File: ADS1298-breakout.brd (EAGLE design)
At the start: 63.5 x 25.4 mm, 31 parts, among them IC2 TPS73250DBVT, IC3 TPS73233DBVT

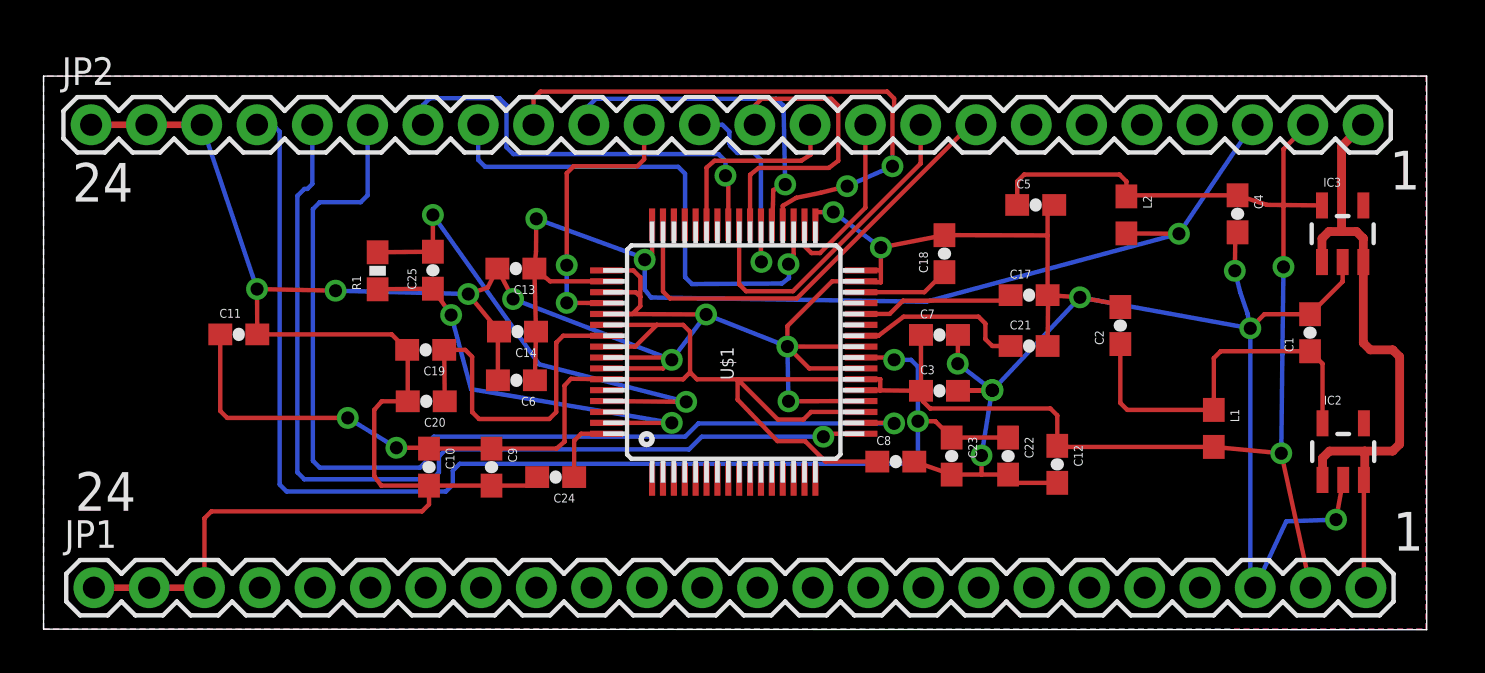
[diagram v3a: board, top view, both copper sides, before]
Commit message: fixed pin spacing so it is 0.1 inch; fixed board outline so it is even on all edges
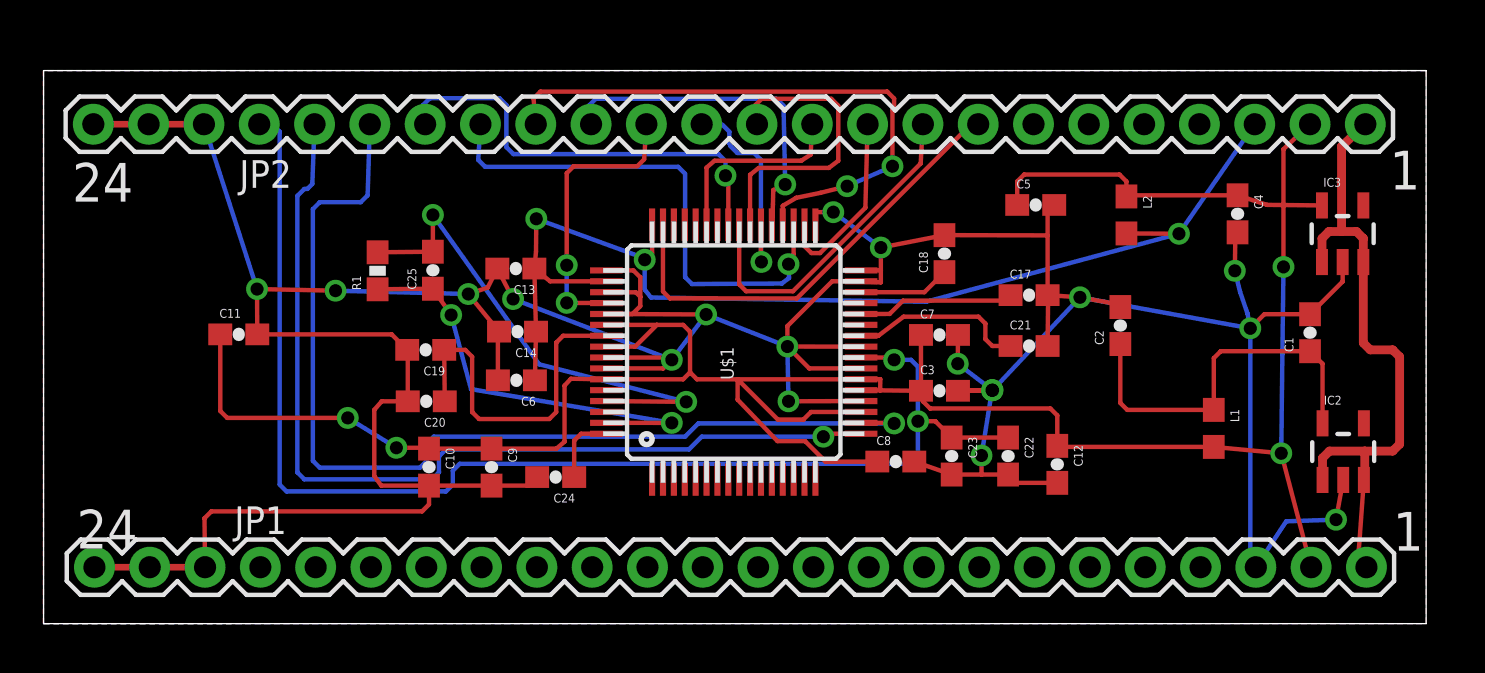
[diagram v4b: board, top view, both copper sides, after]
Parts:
- moved JP1 0.94 mm to (29.0, 2.84)
- moved JP2 0.10 mm to (29.0, 23.2)
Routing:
- net AGND: track 211.2 -> 209.9 mm
- net AVDD: track 107.5 -> 106.7 mm
- net VCC: track 30.4 -> 29.6 mm
- removed copper zone on layer 16, net AGND

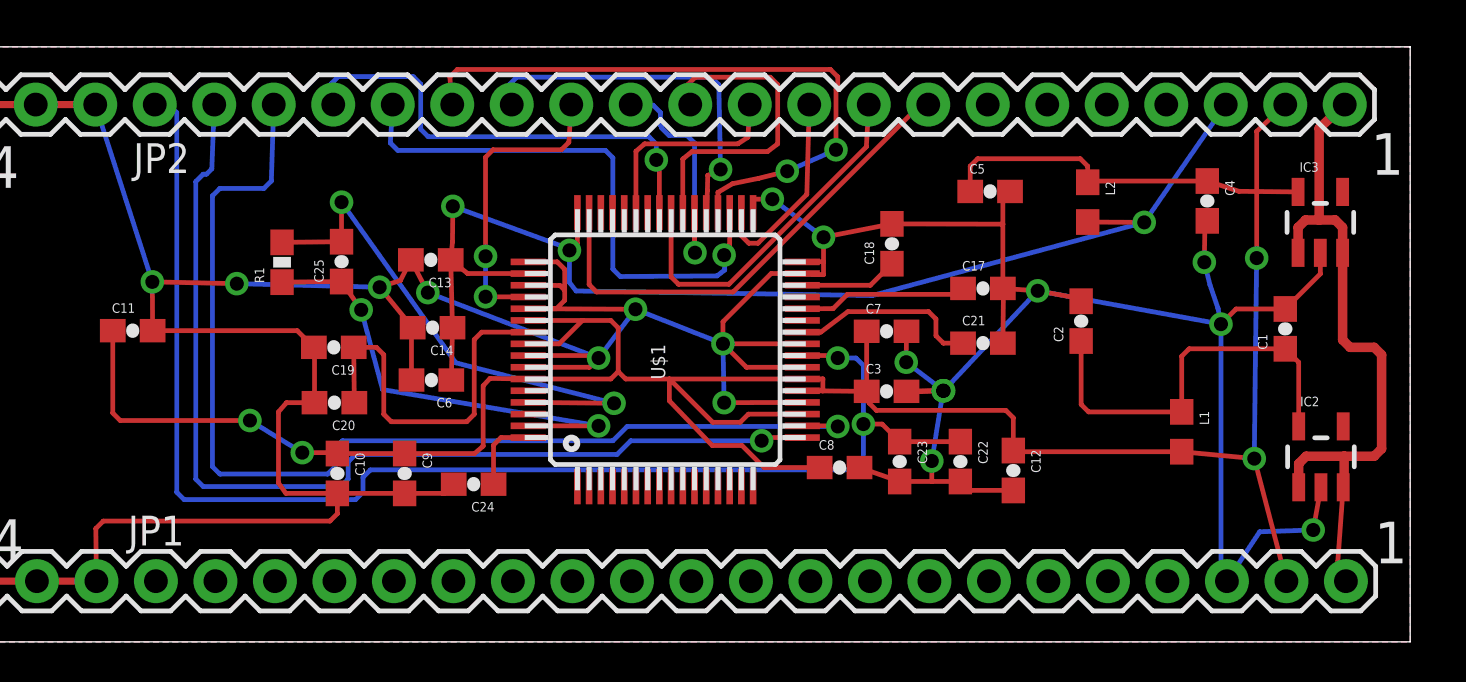
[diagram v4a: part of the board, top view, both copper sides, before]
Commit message: partially routed board passes design rule check; analog ins, GPIOs, and a few other signals still need routing
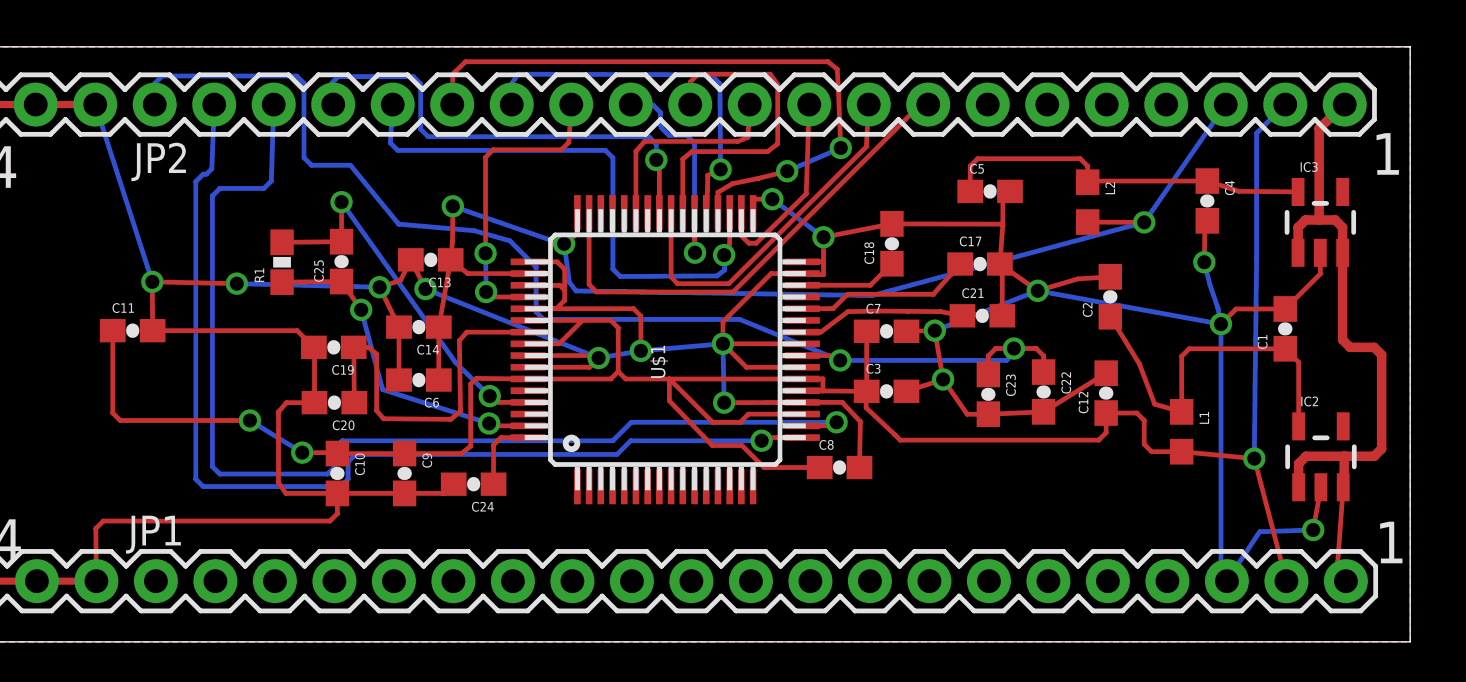
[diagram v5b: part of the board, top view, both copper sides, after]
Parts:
- moved C12 5.16 mm to (50.5, 10.9), turned to 90 degrees
- moved C23 4.75 mm to (45.5, 10.8)
- moved C22 4.63 mm to (47.9, 10.9)
- moved C2 1.62 mm to (50.7, 15.0)
- moved C21 1.17 mm to (45.2, 14.2)
- moved C17 1.05 mm to (45.1, 16.4)
- moved C14 0.58 mm to (21.2, 13.7)
- moved C6 0.53 mm to (21.2, 11.4)
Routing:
- net VREFP: track 59.4 -> 51.4 mm
- net RLD_INV: track 23.3 -> 16.4 mm
- net RLD_OUT: track 19.9 -> 14.0 mm
- net N$2: track 17.6 -> 15.9 mm
- net AVDD: track 106.7 -> 108.1 mm, vias 4 -> 3
- net N$8: track 8.13 -> 7.15 mm
- net AGND: track 209.9 -> 210.0 mm, vias 18 -> 16

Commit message: analog ins are routed - GPIOs still need to be routed
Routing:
- net RLD_REF: track 0.00 -> 39.9 mm, vias 0 -> 1
- net AGND: track 210.0 -> 246.0 mm
- net RLD_IN: track 0.00 -> 31.3 mm, vias 0 -> 1
- net IN8N: track 0.00 -> 21.7 mm
- net IN8P: track 0.00 -> 19.6 mm
- net IN7N: track 0.00 -> 17.6 mm
- net IN7P: track 0.00 -> 15.5 mm
- net IN1P: track 0.00 -> 14.6 mm
- net IN6N: track 0.00 -> 13.5 mm
- net IN1N: track 0.00 -> 12.7 mm
- net IN6P: track 0.00 -> 11.5 mm
- net IN2P: track 0.00 -> 10.7 mm
- net IN5N: track 0.00 -> 9.24 mm, vias 0 -> 1
- net IN2N: track 0.00 -> 8.68 mm
- net IN5P: track 0.00 -> 6.99 mm, vias 0 -> 1
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- added copper zone on layer 16, net AGND
- removed copper zone on layer 16, net N$9

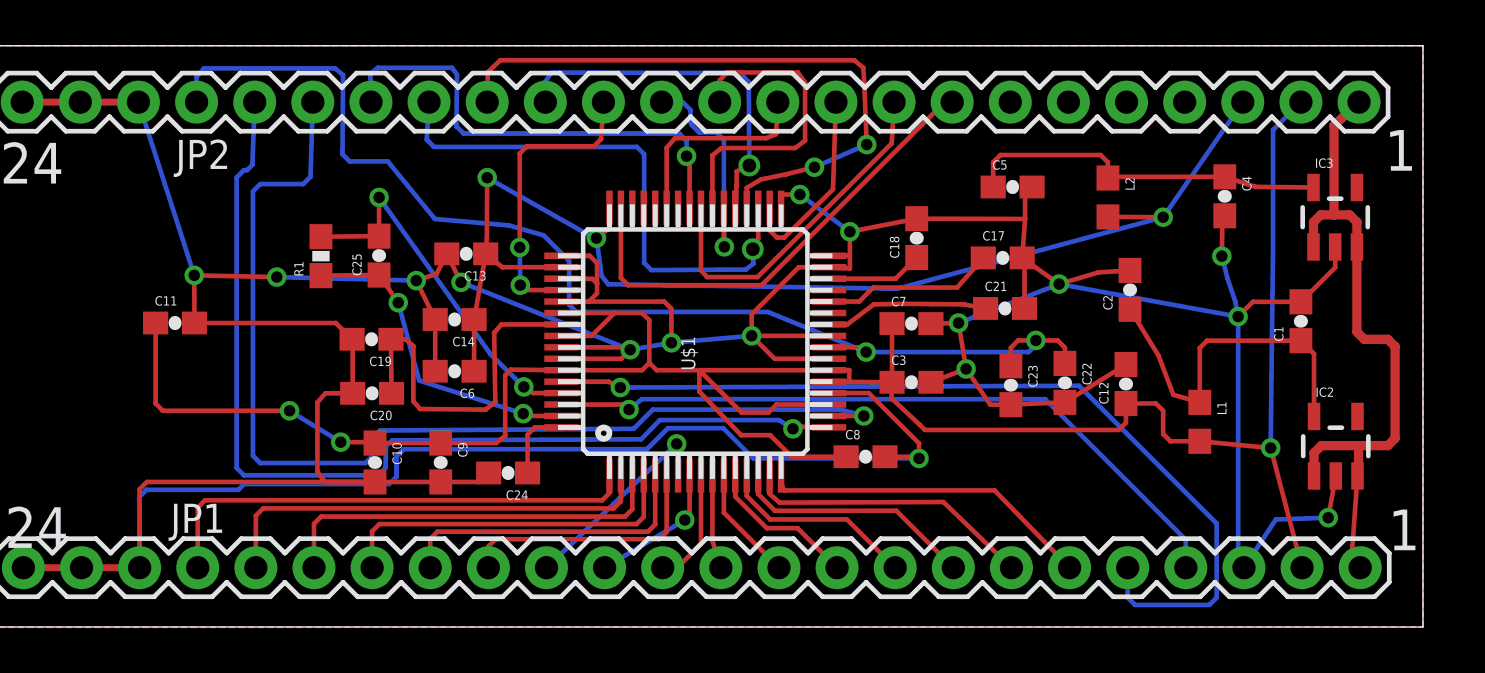
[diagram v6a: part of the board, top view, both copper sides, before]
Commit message: board completely routed, passes design rule check
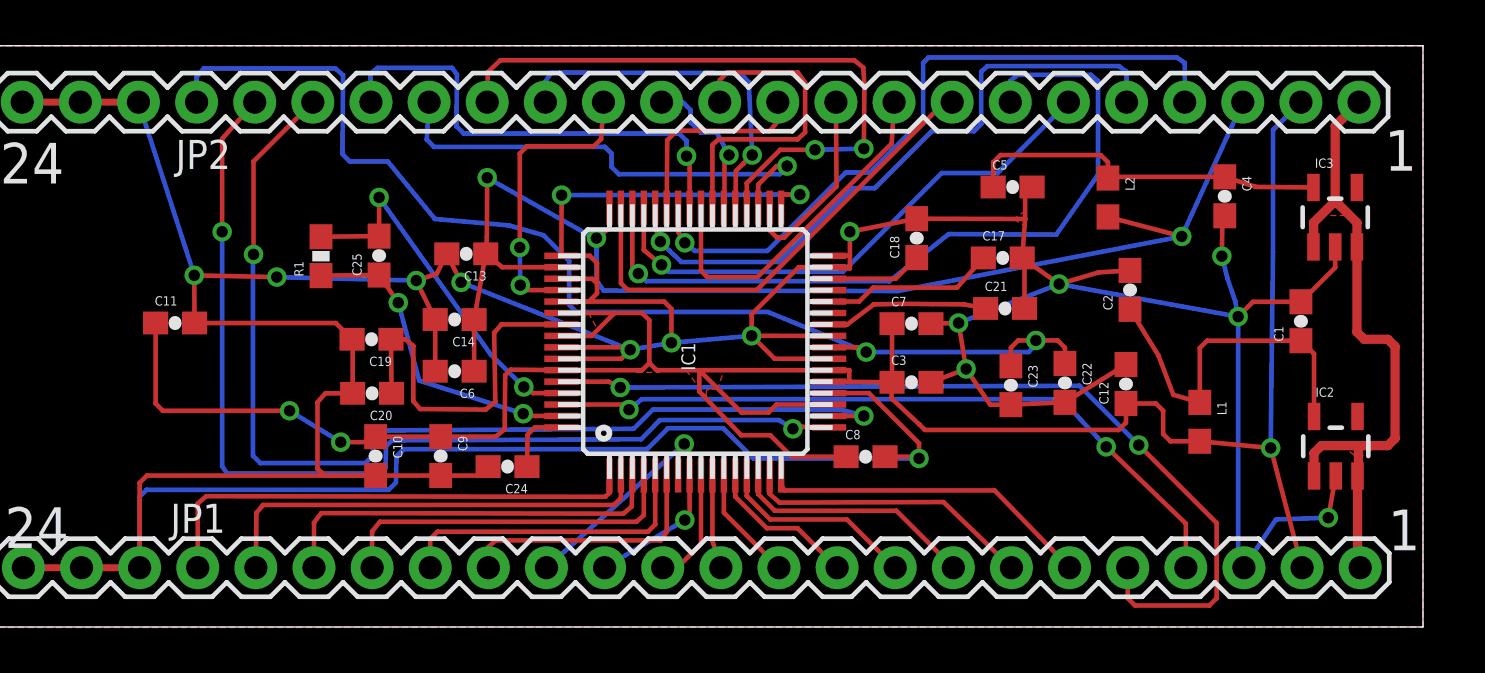
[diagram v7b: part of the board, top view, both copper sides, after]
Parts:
- moved C10 0.28 mm to (17.7, 7.72)
- moved C24 0.28 mm to (23.5, 7.26)
- moved C9 0.28 mm to (20.6, 7.72)
- renumbered U$1 to IC1
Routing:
- net GPIO4: track 0.00 -> 34.4 mm, vias 0 -> 1
- net GPIO1: track 0.00 -> 30.3 mm, vias 0 -> 1
- net GPIO2: track 0.00 -> 28.5 mm, vias 0 -> 1
- net GPIO3: track 0.00 -> 23.8 mm, vias 0 -> 1
- net AGND: track 246.0 -> 256.6 mm, vias 16 -> 17
- net !PWDN: track 23.7 -> 21.1 mm
- net DVDD: track 54.4 -> 56.8 mm
- net SPI_START: track 10.2 -> 8.34 mm
- net PACEOUT2: track 47.4 -> 46.3 mm, vias 1 -> 2
- net IN5P: track 6.99 -> 6.11 mm
- net PACEOUT1: track 44.0 -> 44.7 mm, vias 1 -> 2
- net RLD_IN: track 31.3 -> 31.7 mm, vias 1 -> 2
- net RLD_REF: vias 1 -> 2
- added copper zone on layer 1, net AGND
- added copper zone on layer 1, net AVDD
- added copper zone on layer 1, net VCC

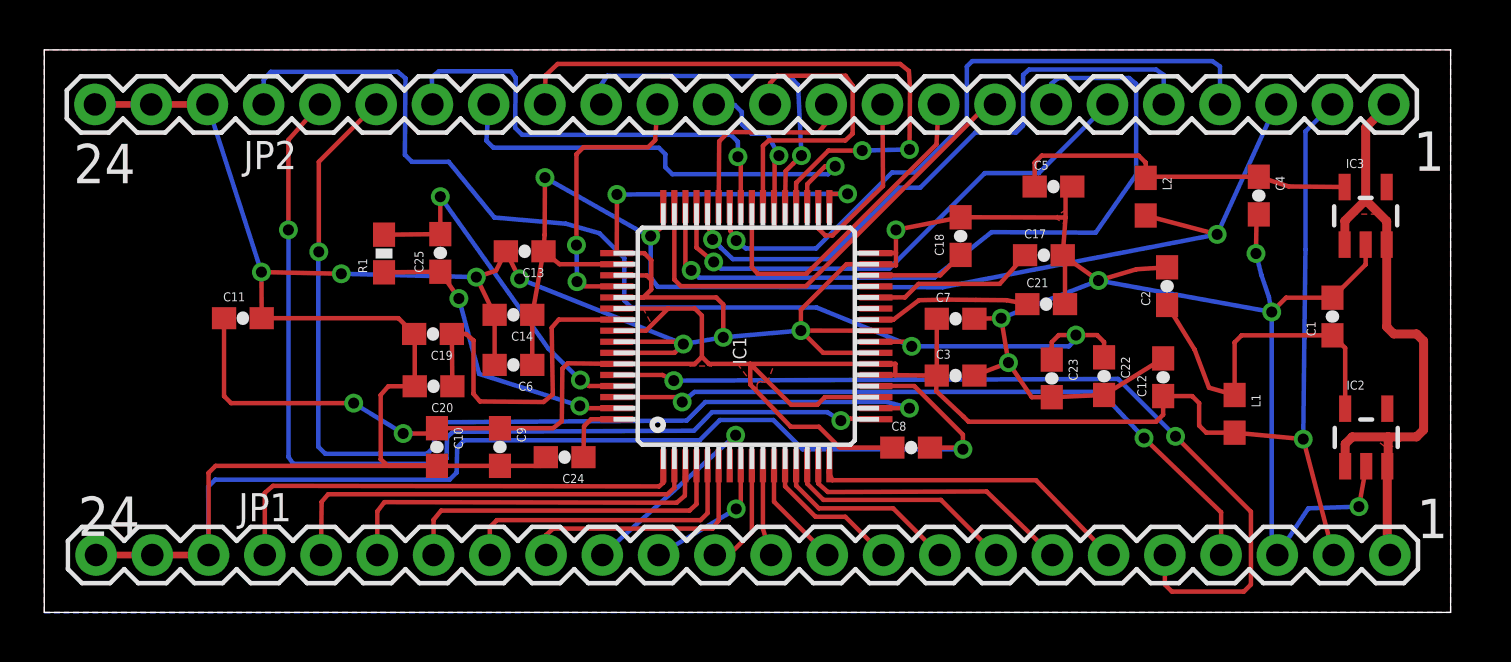
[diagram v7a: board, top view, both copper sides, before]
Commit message: changed via drill holes to be 0.020 inch, compatible with AP Circuits
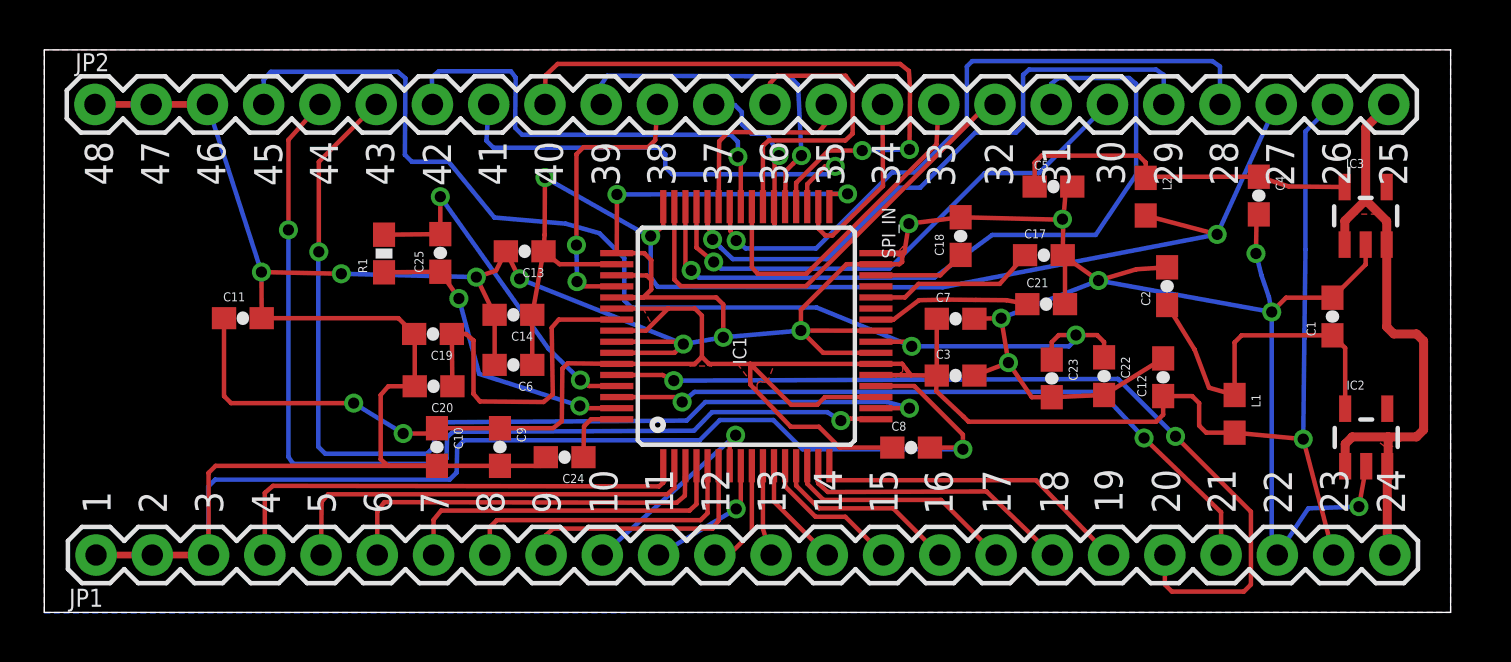
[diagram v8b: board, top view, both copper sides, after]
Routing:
- net AGND: track 256.6 -> 257.4 mm, vias 17 -> 18
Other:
- board text added: "10"
- board text added: "11"
- board text added: "12"
- board text added: "13"
- board text added: "14"
- board text added: "15"
- board text added: "16"
- board text added: "17"
- board text added: "18"
- board text added: "19"
- board text added: "2"
- board text added: "20"
- board text added: "21"
- board text added: "22"
- board text added: "23"
- board text added: "25"
- board text added: "26"
- board text added: "27"
- board text added: "28"
- board text added: "29"
- board text added: "3"
- board text added: "30"
- board text added: "31"
- board text added: "32"
- board text added: "33"
- board text added: "34"
- board text added: "35"
- board text added: "36"
- board text added: "37"
- board text added: "38"
- board text added: "39"
- board text added: "4"
- board text added: "40"
- board text added: "41"
- board text added: "42"
- board text added: "43"
- board text added: "44"
- board text added: "45"
- board text added: "46"
- board text added: "47"
- board text added: "48"
- board text added: "5"
- board text added: "6"
- board text added: "7"
- board text added: "8"
- board text added: "9"
- board text added: "ADS1298 Breakout v0.1"
- board text added: "SPI_IN"
